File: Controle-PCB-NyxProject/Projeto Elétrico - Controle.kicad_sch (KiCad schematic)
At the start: 9 parts, among them J1 Power Supply, J2 Conn_01x03_Male, J3 Conn_01x03_Male, U1 ESP32-DEVKIT-V1, U2 MINI560-StepDown_5v, U3 FlashMemory_W25Q128, U4 GY-521 - Sensor 1, U5 GY-521 - Sensor 2, U6 GY-BMP280

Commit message: -m uploads on PCB and Schematic projects
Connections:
- net PWM 1: now also J2.1 (Pin_1); no longer J2.2 (Pin_2)
- net PWM 2: now also J3.1 (Pin_1); no longer J3.2 (Pin_2)
- net step_5v+: now also J2.2 (Pin_2), J3.2 (Pin_2); no longer J2.1 (Pin_1), J3.1 (Pin_1)
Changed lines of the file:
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@@
     (effects (font (size 1.27 1.27)) (justify left bottom))
   )
-  (label "step_5v+" (at 147.32 171.45 180)
+  (label "PWM 2" (at 147.32 171.45 180)
     (effects (font (size 1.27 1.27)) (justify right bottom))
   )
@@
     (effects (font (size 1.27 1.27)) (justify left bottom))
   )
-  (label "step_5v+" (at 147.32 139.7 180)
+  (label "PWM 1" (at 147.32 139.7 180)
     (effects (font (size 1.27 1.27)) (justify right bottom))
   )
@@
     (effects (font (size 1.27 1.27)) (justify right bottom))
   )
-  (label "PWM 2" (at 147.32 173.99 180)
+  (label "step_5v+" (at 147.32 173.99 180)
     (effects (font (size 1.27 1.27)) (justify right bottom))
   )
@@
     (effects (font (size 1.27 1.27)) (justify left bottom))
   )
-  (label "PWM 1" (at 147.32 142.24 180)
+  (label "step_5v+" (at 147.32 142.24 180)
     (effects (font (size 1.27 1.27)) (justify right bottom))
   )

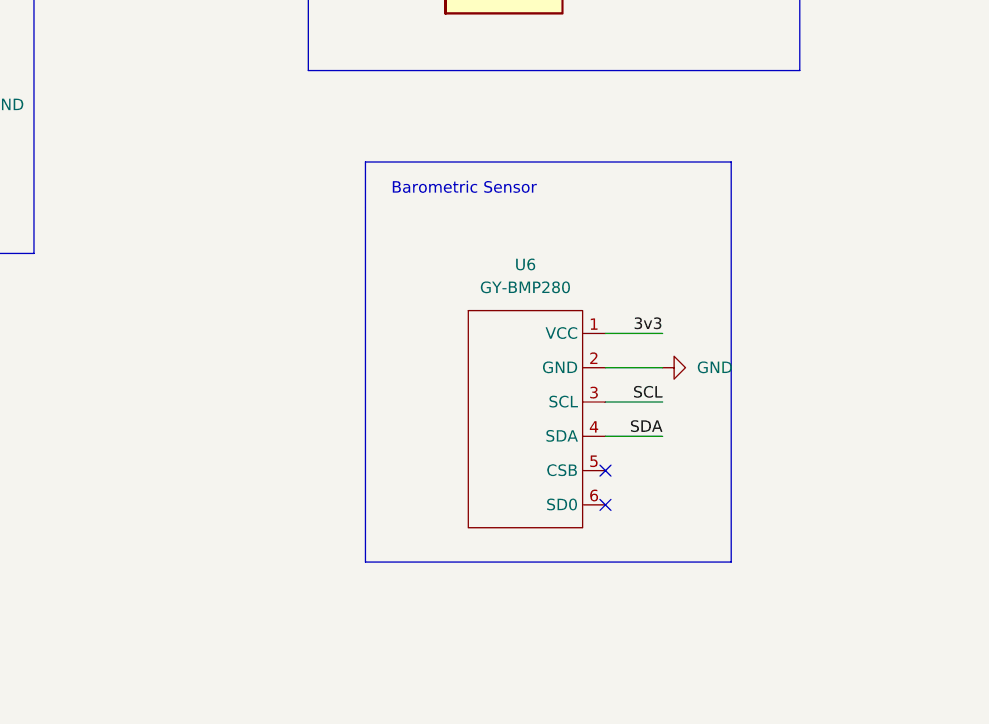
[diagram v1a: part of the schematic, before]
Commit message: Pull-up Resistors added.
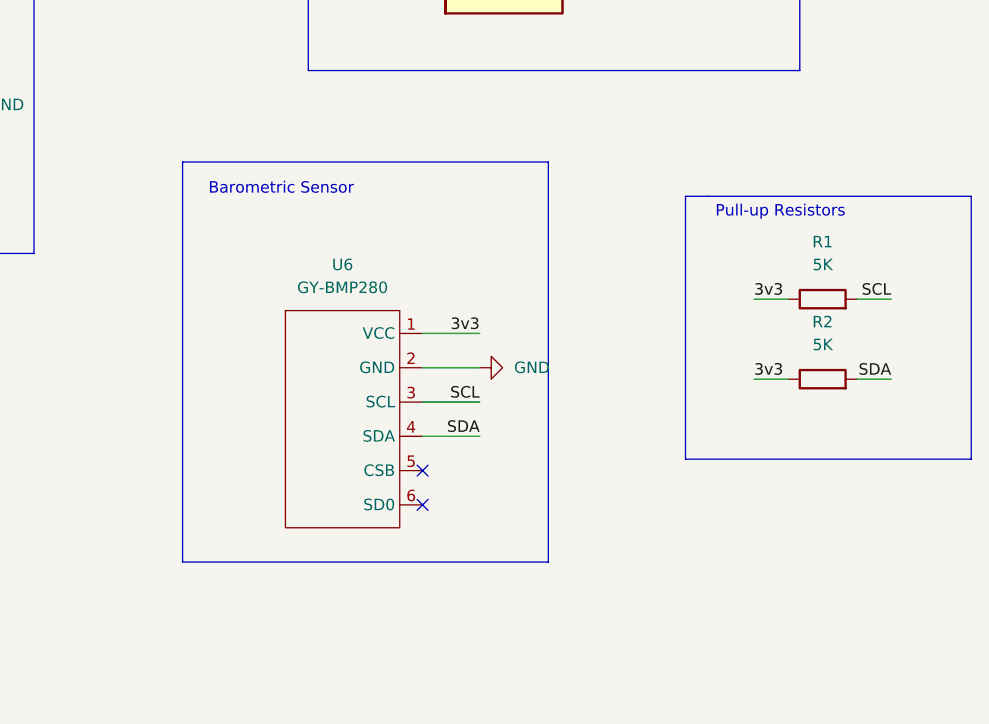
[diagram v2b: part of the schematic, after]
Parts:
- added R1, R2: 5K, Resistor_THT:R_Axial_DIN0204_L3.6mm_D1.6mm_P7.62mm_Horizontal, symbol Device:R
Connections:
- net 3v3: now also R1.1, R2.1
- net SCL: now also R1.2
- net SDA: now also R2.2
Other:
- note added: "Pull-up Resistors"
- moved on the sheet: U6
